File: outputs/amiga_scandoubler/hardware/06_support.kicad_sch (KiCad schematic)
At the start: 22 parts, among them Y1 27MHz ECS-3225MVLC

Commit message: v030wip: R37–R40 を 0402 化してプルアップ／プルダウンを接続(課題2完了)
- 0603 では空き領域に収まらないため、利用者判断で R_0402_1005Metric に変更
- 4 本を縦置き 0.95mm ピッチで配置し、信号ビアを各 B.Cu 配線上へ
- 3V3/GND は面へのビア(R37 は R38 の 3V3 ビアを共用)
- 回路図・ネットリスト・circuit_manifest のフットプリント欄を更新
- KiCad 7 DRC: エラー 0、未接続 106→98。導通確認済み、電源監査 PASS

Co-Authored-By: Claude Opus 5.5 <noreply@anthropic.com>
Claude-Session: https://claude.ai/code/session_019f929sAJ7LRnJRRFvA6g9F
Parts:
- R37, R38, R39, R40: footprint Resistor_SMD:R_0603_1608Metric -> Resistor_SMD:R_0402_1005Metric
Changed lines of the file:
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@@
 (property "Reference" "R37" (id 0) (at 65 228 0) (effects (font (size 1.0 1.0)) ))
 (property "Value" "2.2k" (id 1) (at 65 230.8 0) (effects (font (size 1.0 1.0)) ))
-(property "Footprint" "Resistor_SMD:R_0603_1608Metric" (id 2) (at 65 230.8 0) (effects (font (size 1.0 1.0)) hide))
+(property "Footprint" "Resistor_SMD:R_0402_1005Metric" (id 2) (at 65 230.8 0) (effects (font (size 1.0 1.0)) hide))
 (property "Datasheet" "" (id 3) (at 65 230.8 0) (effects (font (size 1.0 1.0)) hide))
 (property "MPN" "2.2k" (id 4) (at 65 230.8 0) (effects (font (size 1.0 1.0)) hide))
@@
 (property "Reference" "R38" (id 0) (at 159 228 0) (effects (font (size 1.0 1.0)) ))
 (property "Value" "2.2k" (id 1) (at 159 230.8 0) (effects (font (size 1.0 1.0)) ))
-(property "Footprint" "Resistor_SMD:R_0603_1608Metric" (id 2) (at 159 230.8 0) (effects (font (size 1.0 1.0)) hide))
+(property "Footprint" "Resistor_SMD:R_0402_1005Metric" (id 2) (at 159 230.8 0) (effects (font (size 1.0 1.0)) hide))
 (property "Datasheet" "" (id 3) (at 159 230.8 0) (effects (font (size 1.0 1.0)) hide))
 (property "MPN" "2.2k" (id 4) (at 159 230.8 0) (effects (font (size 1.0 1.0)) hide))
@@
 (property "Reference" "R39" (id 0) (at 253 228 0) (effects (font (size 1.0 1.0)) ))
 (property "Value" "10k" (id 1) (at 253 230.8 0) (effects (font (size 1.0 1.0)) ))
-(property "Footprint" "Resistor_SMD:R_0603_1608Metric" (id 2) (at 253 230.8 0) (effects (font (size 1.0 1.0)) hide))
+(property "Footprint" "Resistor_SMD:R_0402_1005Metric" (id 2) (at 253 230.8 0) (effects (font (size 1.0 1.0)) hide))
 (property "Datasheet" "" (id 3) (at 253 230.8 0) (effects (font (size 1.0 1.0)) hide))
 (property "MPN" "10k" (id 4) (at 253 230.8 0) (effects (font (size 1.0 1.0)) hide))
@@
 (property "Reference" "R40" (id 0) (at 347 228 0) (effects (font (size 1.0 1.0)) ))
 (property "Value" "10k" (id 1) (at 347 230.8 0) (effects (font (size 1.0 1.0)) ))
-(property "Footprint" "Resistor_SMD:R_0603_1608Metric" (id 2) (at 347 230.8 0) (effects (font (size 1.0 1.0)) hide))
+(property "Footprint" "Resistor_SMD:R_0402_1005Metric" (id 2) (at 347 230.8 0) (effects (font (size 1.0 1.0)) hide))
 (property "Datasheet" "" (id 3) (at 347 230.8 0) (effects (font (size 1.0 1.0)) hide))
 (property "MPN" "10k" (id 4) (at 347 230.8 0) (effects (font (size 1.0 1.0)) hide))
@@
 (path "/d7285cc1-01a7-52b5-b1b4-a16a6a4410c1/e4a3674d-f2c7-595e-9f91-66c1d923f533/06031825-fe01-59ff-af9d-7a176aec3190" (reference "C68") (unit 1) (value "4.7uF") (footprint "Capacitor_SMD:C_0805_2012Metric"))
 (path "/d7285cc1-01a7-52b5-b1b4-a16a6a4410c1/e4a3674d-f2c7-595e-9f91-66c1d923f533/032716d6-b85b-5cd6-b9fb-a0db9fcdc04a" (reference "C69") (unit 1) (value "100nF") (footprint "Capacitor_SMD:C_0603_1608Metric"))
-(path "/d7285cc1-01a7-52b5-b1b4-a16a6a4410c1/e4a3674d-f2c7-595e-9f91-66c1d923f533/19afe537-a6d6-5fe3-a559-90d2fa10deb2" (reference "R37") (unit 1) (value "2.2k") (footprint "Resistor_SMD:R_0603_1608Metric"))
-(path "/d7285cc1-01a7-52b5-b1b4-a16a6a4410c1/e4a3674d-f2c7-595e-9f91-66c1d923f533/0b53f7f2-1b15-5eb0-a4f2-25c1fe4dc3b2" (reference "R38") (unit 1) (value "2.2k") (footprint "Resistor_SMD:R_0603_1608Metric"))
-(path "/d7285cc1-01a7-52b5-b1b4-a16a6a4410c1/e4a3674d-f2c7-595e-9f91-66c1d923f533/1f6b4e55-3208-511e-bd65-aee29525e886" (reference "R39") (unit 1) (value "10k") (footprint "Resistor_SMD:R_0603_1608Metric"))
-(path "/d7285cc1-01a7-52b5-b1b4-a16a6a4410c1/e4a3674d-f2c7-595e-9f91-66c1d923f533/f3206b5b-9e26-52a8-92e8-c6c786fe557c" (reference "R40") (unit 1) (value "10k") (footprint "Resistor_SMD:R_0603_1608Metric"))
+(path "/d7285cc1-01a7-52b5-b1b4-a16a6a4410c1/e4a3674d-f2c7-595e-9f91-66c1d923f533/19afe537-a6d6-5fe3-a559-90d2fa10deb2" (reference "R37") (unit 1) (value "2.2k") (footprint "Resistor_SMD:R_0402_1005Metric"))
+(path "/d7285cc1-01a7-52b5-b1b4-a16a6a4410c1/e4a3674d-f2c7-595e-9f91-66c1d923f533/0b53f7f2-1b15-5eb0-a4f2-25c1fe4dc3b2" (reference "R38") (unit 1) (value "2.2k") (footprint "Resistor_SMD:R_0402_1005Metric"))
+(path "/d7285cc1-01a7-52b5-b1b4-a16a6a4410c1/e4a3674d-f2c7-595e-9f91-66c1d923f533/1f6b4e55-3208-511e-bd65-aee29525e886" (reference "R39") (unit 1) (value "10k") (footprint "Resistor_SMD:R_0402_1005Metric"))
+(path "/d7285cc1-01a7-52b5-b1b4-a16a6a4410c1/e4a3674d-f2c7-595e-9f91-66c1d923f533/f3206b5b-9e26-52a8-92e8-c6c786fe557c" (reference "R40") (unit 1) (value "10k") (footprint "Resistor_SMD:R_0402_1005Metric"))
 (path "/d7285cc1-01a7-52b5-b1b4-a16a6a4410c1/e4a3674d-f2c7-595e-9f91-66c1d923f533/4bdee17e-e346-5574-b8f0-9c516d59ea80" (reference "R41") (unit 1) (value "10k") (footprint "Resistor_SMD:R_0603_1608Metric"))
 (path "/d7285cc1-01a7-52b5-b1b4-a16a6a4410c1/e4a3674d-f2c7-595e-9f91-66c1d923f533/df75f8ac-b9ae-5e0b-a8f0-d2245b09bd47" (reference "R42") (unit 1) (value "10k") (footprint "Resistor_SMD:R_0603_1608Metric"))

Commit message: Select LCSC parts with live JLCPCB stock/price (135 of 139 parts)
- r11_select.py queries JLCPCB's public component search. It matches package and spec (C/V/dielectric, R/tolerance, 0.1% thin film) and ranks basic > preferred > stock.
- Results are in fab/v030wip/parts_selection.csv/.json. r11_apply.py writes LCSC/MPN into the manifest, schematic symbols and netlist.
- Open items:
  - U1 TVP7002: stock 4.
  - J1/J2 CONEC 33DSMT1-E15SNCT: stock 0.
  - Y1 ECS-3225MVLC-270: stock 4. YXC OT2EL4C4JI-111OLP-27M (C5203549) is a datasheet-checked drop-in candidate.
- Nets unchanged (595 nodes match the board). The audit passes. Nothing ordered.

Co-Authored-By: Claude Opus 5.5 <noreply@anthropic.com>
Claude-Session: https://claude.ai/code/session_019f929sAJ7LRnJRRFvA6g9F
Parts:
- C61, C63, C65, C67, C69: LCSC (none) -> C14663; MPN 100nF -> CC0603KRX7R9BB104
- C62, C64, C66, C68: LCSC (none) -> C1779; MPN 4.7uF -> CL21A475KAQNNNE
- FB1, FB2, FB3, FB4: LCSC (none) -> C304314; MPN 220R@100MHz -> HCB1608KF-221T20
- R36: LCSC (none) -> C23345; MPN 22R -> 0603WAF220JT5E
- R37, R38: LCSC (none) -> C25879; MPN 2.2k -> 0402WGF2201TCE
- R39, R40: LCSC (none) -> C25744; MPN 10k -> 0402WGF1002TCE
- R41, R42, R43: LCSC (none) -> C25804; MPN 10k -> 0603WAF1002T5E

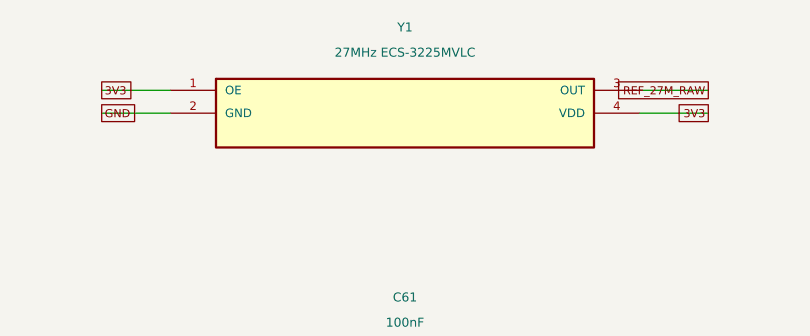
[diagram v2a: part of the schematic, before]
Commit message: Replace Y1 with YXC OT2EL4C4JI-111OLP-27M; reselect parts for 2 boards
- Y1: ECS-3225MVLC-270 (LCSC stock 4) -> C5203549, a pin/land-compatible 3225 CMOS oscillator (datasheet checked). Footprint and routing unchanged.
- Selection re-run for a 2-board build (JLCPCB PCBA minimum is 2). U1 is covered (stock 4). J1/J2 carry C3146802 for Global Sourcing.
- All 139 parts now have LCSC numbers.
- Nets still match (595 nodes). DRC errors 0, unconnected 0. The audit passes.

Co-Authored-By: Claude Opus 5.5 <noreply@anthropic.com>
Claude-Session: https://claude.ai/code/session_019f929sAJ7LRnJRRFvA6g9F
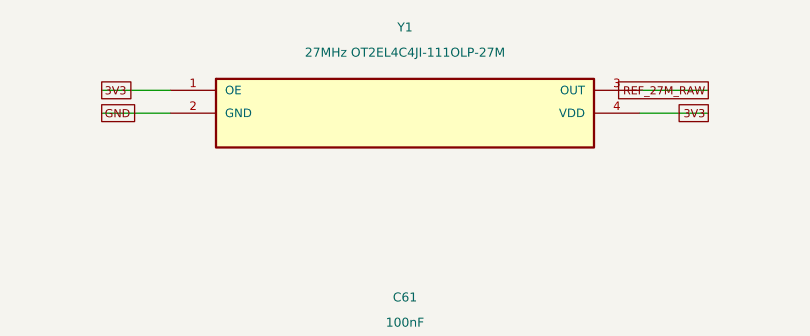
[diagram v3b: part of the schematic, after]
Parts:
- Y1: value 27MHz ECS-3225MVLC -> 27MHz OT2EL4C4JI-111OLP-27M; LCSC (none) -> C5203549; MPN ECS-3225MVLC-270-CN-TR -> OT2EL4C4JI-111OLP-27M
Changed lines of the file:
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@@
 (symbol (lib_id "Amiga:OSC_3225") (at 85 40 0) (unit 1) (in_bom yes) (on_board yes)
 (property "Reference" "Y1" (id 0) (at 85 33 0) (effects (font (size 1.0 1.0)) ))
-(property "Value" "27MHz ECS-3225MVLC" (id 1) (at 85 35.8 0) (effects (font (size 1.0 1.0)) ))
+(property "Value" "27MHz OT2EL4C4JI-111OLP-27M" (id 1) (at 85 35.8 0) (effects (font (size 1.0 1.0)) ))
 (property "Footprint" "Amiga:OSC_ECS-3225MVLC_3.2x2.5" (id 2) (at 85 35.8 0) (effects (font (size 1.0 1.0)) hide))
 (property "Datasheet" "" (id 3) (at 85 35.8 0) (effects (font (size 1.0 1.0)) hide))
-(property "MPN" "ECS-3225MVLC-270-CN-TR" (id 4) (at 85 35.8 0) (effects (font (size 1.0 1.0)) hide))
-(property "LCSC" "" (id 5) (at 85 35.8 0) (effects (font (size 1.0 1.0)) hide))
+(property "MPN" "OT2EL4C4JI-111OLP-27M" (id 4) (at 85 35.8 0) (effects (font (size 1.0 1.0)) hide))
+(property "LCSC" "C5203549" (id 5) (at 85 35.8 0) (effects (font (size 1.0 1.0)) hide))
 (pin "1")
 (pin "2")
@@
 (sheet_instances (path "/" (page "7")))
 (symbol_instances
-(path "/d7285cc1-01a7-52b5-b1b4-a16a6a4410c1/e4a3674d-f2c7-595e-9f91-66c1d923f533/62880021-8bf0-5a67-9574-d03ec8975216" (reference "Y1") (unit 1) (value "27MHz ECS-3225MVLC") (footprint "Amiga:OSC_ECS-3225MVLC_3.2x2.5"))
+(path "/d7285cc1-01a7-52b5-b1b4-a16a6a4410c1/e4a3674d-f2c7-595e-9f91-66c1d923f533/62880021-8bf0-5a67-9574-d03ec8975216" (reference "Y1") (unit 1) (value "27MHz OT2EL4C4JI-111OLP-27M") (footprint "Amiga:OSC_ECS-3225MVLC_3.2x2.5"))
 (path "/d7285cc1-01a7-52b5-b1b4-a16a6a4410c1/e4a3674d-f2c7-595e-9f91-66c1d923f533/3ae81705-2b6e-5f54-8da2-747c927bb610" (reference "R36") (unit 1) (value "22R") (footprint "Resistor_SMD:R_0603_1608Metric"))
 (path "/d7285cc1-01a7-52b5-b1b4-a16a6a4410c1/e4a3674d-f2c7-595e-9f91-66c1d923f533/c2409389-ffe1-5958-ae2d-4922f9560ea9" (reference "C61") (unit 1) (value "100nF") (footprint "Capacitor_SMD:C_0603_1608Metric"))
